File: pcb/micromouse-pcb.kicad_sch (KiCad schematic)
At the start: 40 parts, among them J2 Conn_01x06_EncoderSocket, M1 Motor_DC, Q1 BS170, Q2 TEFT4300, Q3 BS170, Q4 TEFT4300, Q5 BS170, Q6 TEFT4300, Q7 BS170, Q8 TEFT4300, SW1 SW_SPDT, U0 Teensy 4.1, U1 L7805, U2 DRV8833PWP

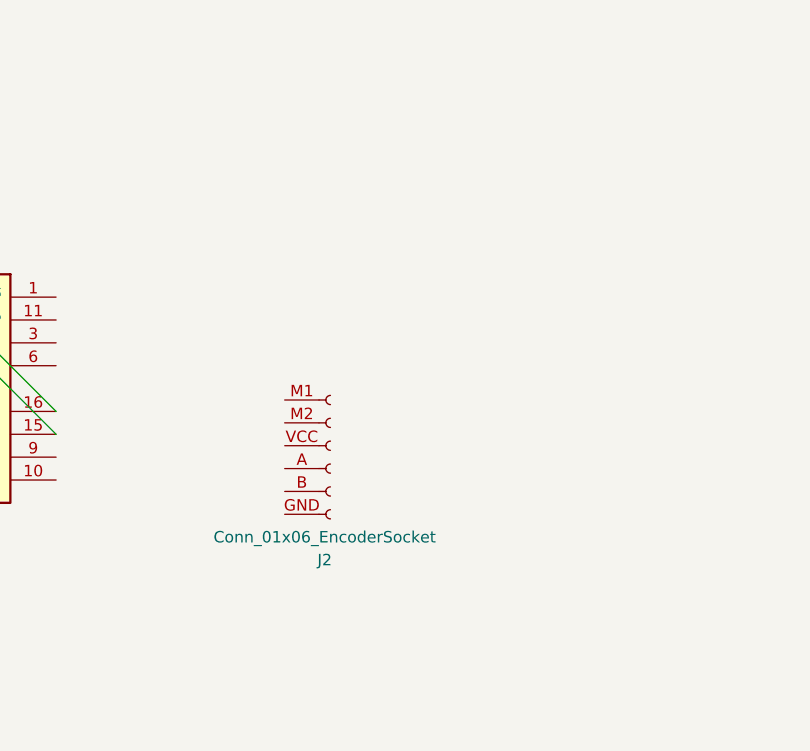
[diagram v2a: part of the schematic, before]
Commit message: changed connectors in motor module
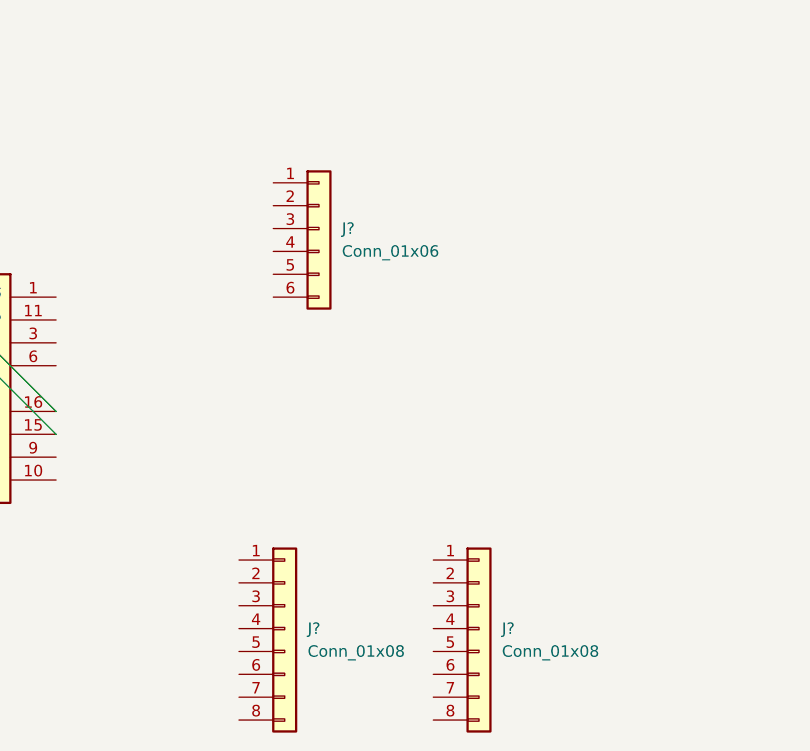
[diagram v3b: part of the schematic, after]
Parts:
- removed J2: Conn_01x06_EncoderSocket, symbol micromouse-symbols:Conn_01x06_EncoderSocket
- added J?: Conn_01x06, symbol Connector_Generic:Conn_01x06
- added J? (x2): Conn_01x08, symbol Connector_Generic:Conn_01x08
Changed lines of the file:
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@@
 	)
 	(symbol
+		(lib_id "Connector_Generic:Conn_01x06")
+		(at 146.05 223.52 0)
+		(unit 1)
+		(exclude_from_sim no)
+		(in_bom yes)
+		(on_board yes)
+		(dnp no)
+		(fields_autoplaced yes)
+		(property "Reference" "J?"
+			(at 148.59 223.5199 0)
+			(effects
+				(font
+					(size 1.27 1.27)
+				)
+				(justify left)
+			)
+		)
+		(property "Value" "Conn_01x06"
+			(at 148.59 226.0599 0)
+			(effects
+				(font
+					(size 1.27 1.27)
+				)
+				(justify left)
+			)
+		)
+		(property "Footprint" ""
+			(at 146.05 223.52 0)
+			(effects
+				(font
+					(size 1.27 1.27)
+				)
+				(hide yes)
+			)
+		)
+		(property "Datasheet" "~"
+			(at 146.05 223.52 0)
+			(effects
+				(font
+					(size 1.27 1.27)
+				)
+				(hide yes)
+			)
+		)
+		(property "Description" "Generic connector, single row, 01x06, script generated (kicad-library-utils/schlib/autogen/connector/)"
+			(at 146.05 223.52 0)
+			(effects
+				(font
+					(size 1.27 1.27)
+				)
+				(hide yes)
+			)
+		)
+		(pin "1"
+		)
+		(pin "4"
+		)
+		(pin "2"
+		)
+		(pin "6"
+		)
+		(pin "5"
+		)
+		(pin "3"
+		)
+		(instances
+			(project ""
+				(path "/6bab3514-b9e6-4652-bd2e-edc57bdbde3d"
+					(reference "J?")
+					(unit 1)
+				)
+			)
+		)
+	)
+	(symbol
 		(lib_id "Regulator_Linear:L7805")
 		(at 346.71 46.99 0)
@@
 	)
 	(symbol
-		(lib_id "micromouse-symbols:Conn_01x06_EncoderSocket")
-		(at 147.32 247.65 0)
+		(lib_id "Transistor_FET:BS170")
+		(at 361.95 120.65 90)
 		(unit 1)
 		(exclude_from_sim no)
@@
 		(on_board yes)
 		(dnp no)
-		(property "Reference" "J2"
-			(at 146.685 260.35 0)
+		(fields_autoplaced yes)
+		(property "Reference" "Q1"
+			(at 361.95 111.76 90)
 			(effects
 				(font
@@
 			)
 		)
-		(property "Value" "Conn_01x06_EncoderSocket"
-			(at 146.685 257.81 0)
+		(property "Value" "BS170"
+			(at 361.95 114.3 90)
 			(effects
 				(font
@@
 			)
 		)
-		(property "Footprint" ""
-			(at 147.32 247.65 0)
+		(property "Footprint" "Package_TO_SOT_THT:TO-92_Inline"
+			(at 363.855 115.57 0)
 			(effects
 				(font
 					(size 1.27 1.27)
+					(italic yes)
 				)
+				(justify left)
 				(hide yes)
 			)
 		)
-		(property "Datasheet" "~"
-			(at 147.32 247.65 0)
+		(property "Datasheet" "https://www.onsemi.com/pub/Collateral/BS170-D.PDF"
+			(at 365.76 115.57 0)
 			(effects
 				(font
 					(size 1.27 1.27)
 				)
+				(justify left)
 				(hide yes)
 			)
 		)
-		(property "Description" "Generic connector, single row, 01x06, script generated"
-			(at 147.32 247.65 0)
+		(property "Description" "0.5A Id, 60V Vds, N-Channel MOSFET, TO-92"
+			(at 361.95 120.65 0)
 			(effects
 				(font
@@
 			)
 		)
-		(pin "A"
-		)
-		(pin "B"
-		)
-		(pin "GND"
-		)
-		(pin "M1"
+		(pin "1"
 		)
-		(pin "M2"
+		(pin "2"
 		)
-		(pin "VCC"
+		(pin "3"
 		)
 		(instances
 			(project ""
 				(path "/6bab3514-b9e6-4652-bd2e-edc57bdbde3d"
-					(reference "J2")
+					(reference "Q1")
 					(unit 1)
 				)
@@
 	)
 	(symbol
-		(lib_id "Transistor_FET:BS170")
-		(at 361.95 120.65 90)
+		(lib_id "power:GND")
+		(at 346.71 59.69 0)
 		(unit 1)
 		(exclude_from_sim no)
@@
 		(dnp no)
 		(fields_autoplaced yes)
-		(property "Reference" "Q1"
-			(at 361.95 111.76 90)
+		(property "Reference" "#PWR01"
+			(at 346.71 66.04 0)
 			(effects
 				(font
 					(size 1.27 1.27)
 				)
+				(hide yes)
 			)
 		)
-		(property "Value" "BS170"
-			(at 361.95 114.3 90)
+		(property "Value" "GND"
+			(at 349.25 60.9599 0)
 			(effects
 				(font
 					(size 1.27 1.27)
 				)
+				(justify left)
 			)
 		)
-		(property "Footprint" "Package_TO_SOT_THT:TO-92_Inline"
-			(at 363.855 115.57 0)
+		(property "Footprint" ""
+			(at 346.71 59.69 0)
 			(effects
 				(font
 					(size 1.27 1.27)
-					(italic yes)
 				)
-				(justify left)
 				(hide yes)
 			)
 		)
-		(property "Datasheet" "https://www.onsemi.com/pub/Collateral/BS170-D.PDF"
-			(at 365.76 115.57 0)
+		(property "Datasheet" ""
+			(at 346.71 59.69 0)
 			(effects
 				(font
 					(size 1.27 1.27)
 				)
-				(justify left)
 				(hide yes)
 			)
 		)
-		(property "Description" "0.5A Id, 60V Vds, N-Channel MOSFET, TO-92"
-			(at 361.95 120.65 0)
+		(property "Description" "Power symbol creates a global label with name \"GND\" , ground"
+			(at 346.71 59.69 0)
 			(effects
 				(font
@@
 		(pin "1"
 		)
-		(pin "2"
-		)
-		(pin "3"
-		)
 		(instances
 			(project ""
 				(path "/6bab3514-b9e6-4652-bd2e-edc57bdbde3d"
-					(reference "Q1")
+					(reference "#PWR01")
 					(unit 1)
 				)
@@
 	)
 	(symbol
-		(lib_id "power:GND")
-		(at 346.71 59.69 0)
+		(lib_id "Connector_Generic:Conn_01x08")
+		(at 163.83 267.97 0)
 		(unit 1)
 		(exclude_from_sim no)
@@
 		(dnp no)
 		(fields_autoplaced yes)
-		(property "Reference" "#PWR01"
-			(at 346.71 66.04 0)
+		(property "Reference" "J?"
+			(at 166.37 267.9699 0)
 			(effects
 				(font
 					(size 1.27 1.27)
 				)
-				(hide yes)
+				(justify left)
 			)
 		)
-		(property "Value" "GND"
-			(at 349.25 60.9599 0)
+		(property "Value" "Conn_01x08"
+			(at 166.37 270.5099 0)
 			(effects
 				(font
@@
 		)
 		(property "Footprint" ""
-			(at 346.71 59.69 0)
+			(at 163.83 267.97 0)
 			(effects
 				(font
@@
 			)
 		)
-		(property "Datasheet" ""
-			(at 346.71 59.69 0)
+		(property "Datasheet" "~"
+			(at 163.83 267.97 0)
 			(effects
 				(font
@@
 			)
 		)
-		(property "Description" "Power symbol creates a global label with name \"GND\" , ground"
-			(at 346.71 59.69 0)
+		(property "Description" "Generic connector, single row, 01x08, script generated (kicad-library-utils/schlib/autogen/connector/)"
+			(at 163.83 267.97 0)
 			(effects
 				(font
@@
 			)
 		)
+		(pin "2"
+		)
+		(pin "3"
+		)
+		(pin "4"
+		)
+		(pin "5"
+		)
+		(pin "6"
+		)
+		(pin "7"
+		)
+		(pin "8"
+		)
 		(pin "1"
 		)
@@
 			(project ""
 				(path "/6bab3514-b9e6-4652-bd2e-edc57bdbde3d"
-					(reference "#PWR01")
+					(reference "J?")
 					(unit 1)
 				)
@@
 					(unit 1)
 				)
+			)
+		)
+	)
+	(symbol
+		(lib_id "Connector_Generic:Conn_01x08")
+		(at 142.24 267.97 0)
+		(unit 1)
+		(exclude_from_sim no)
+		(in_bom yes)
+		(on_board yes)
+		(dnp no)
+		(fields_autoplaced yes)
+		(property "Reference" "J?"
+			(at 144.78 267.9699 0)
+			(effects
+				(font
+					(size 1.27 1.27)
+				)
+				(justify left)
+			)
+		)
+		(property "Value" "Conn_01x08"
+			(at 144.78 270.5099 0)
+			(effects
+				(font
+					(size 1.27 1.27)
+				)
+				(justify left)
+			)
+		)
+		(property "Footprint" ""
+			(at 142.24 267.97 0)
+			(effects
+				(font
+					(size 1.27 1.27)
+				)
+				(hide yes)
+			)
+		)
+		(property "Datasheet" "~"
+			(at 142.24 267.97 0)
+			(effects
+				(font
+					(size 1.27 1.27)
+				)
+				(hide yes)
+			)
+		)
+		(property "Description" "Generic connector, single row, 01x08, script generated (kicad-library-utils/schlib/autogen/connector/)"
+			(at 142.24 267.97 0)
+			(effects
+				(font
+					(size 1.27 1.27)
+				)
+				(hide yes)
+			)
+		)
+		(pin "2"
+		)
+		(pin "3"
+		)
+		(pin "4"
+		)
+		(pin "5"
+		)
+		(pin "6"
+		)
+		(pin "7"
+		)
+		(pin "8"
+		)
+		(pin "1"
+		)
+		(instances
+			(project "micromouse-pcb"
+				(path "/6bab3514-b9e6-4652-bd2e-edc57bdbde3d"
+					(reference "J?")
+					(unit 1)
+				)

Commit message: schematic not updating?
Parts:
- gave numbers to parts that had none: 3
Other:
- moved on the sheet: J2, J3
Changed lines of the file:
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@@
 		(dnp no)
 		(fields_autoplaced yes)
-		(property "Reference" "J?"
+		(property "Reference" "J1"
 			(at 148.59 223.5199 0)
 			(effects
@@
 			(project ""
 				(path "/6bab3514-b9e6-4652-bd2e-edc57bdbde3d"
-					(reference "J?")
+					(reference "J1")
 					(unit 1)
 				)
@@
 	(symbol
 		(lib_id "Connector_Generic:Conn_01x08")
-		(at 163.83 267.97 0)
+		(at 168.91 254 0)
 		(unit 1)
 		(exclude_from_sim no)
@@
 		(dnp no)
 		(fields_autoplaced yes)
-		(property "Reference" "J?"
-			(at 166.37 267.9699 0)
+		(property "Reference" "J3"
+			(at 171.45 253.9999 0)
 			(effects
 				(font
@@
 		)
 		(property "Value" "Conn_01x08"
-			(at 166.37 270.5099 0)
+			(at 171.45 256.5399 0)
 			(effects
 				(font
@@
 		)
 		(property "Footprint" ""
-			(at 163.83 267.97 0)
+			(at 168.91 254 0)
 			(effects
 				(font
@@
 		)
 		(property "Datasheet" "~"
-			(at 163.83 267.97 0)
+			(at 168.91 254 0)
 			(effects
 				(font
@@
 		)
 		(property "Description" "Generic connector, single row, 01x08, script generated (kicad-library-utils/schlib/autogen/connector/)"
-			(at 163.83 267.97 0)
+			(at 168.91 254 0)
 			(effects
 				(font
@@
 			(project ""
 				(path "/6bab3514-b9e6-4652-bd2e-edc57bdbde3d"
-					(reference "J?")
+					(reference "J3")
 					(unit 1)
 				)
@@
 	(symbol
 		(lib_id "Connector_Generic:Conn_01x08")
-		(at 142.24 267.97 0)
+		(at 142.24 254 0)
 		(unit 1)
 		(exclude_from_sim no)
@@
 		(dnp no)
 		(fields_autoplaced yes)
-		(property "Reference" "J?"
-			(at 144.78 267.9699 0)
+		(property "Reference" "J2"
+			(at 144.78 253.9999 0)
 			(effects
 				(font
@@
 		)
 		(property "Value" "Conn_01x08"
-			(at 144.78 270.5099 0)
+			(at 144.78 256.5399 0)
 			(effects
 				(font
@@
 		)
 		(property "Footprint" ""
-			(at 142.24 267.97 0)
+			(at 142.24 254 0)
 			(effects
 				(font
@@
 		)
 		(property "Datasheet" "~"
-			(at 142.24 267.97 0)
+			(at 142.24 254 0)
 			(effects
 				(font
@@
 		)
 		(property "Description" "Generic connector, single row, 01x08, script generated (kicad-library-utils/schlib/autogen/connector/)"
-			(at 142.24 267.97 0)
+			(at 142.24 254 0)
 			(effects
 				(font
@@
 			(project "micromouse-pcb"
 				(path "/6bab3514-b9e6-4652-bd2e-edc57bdbde3d"
-					(reference "J?")
+					(reference "J2")
 					(unit 1)
 				)

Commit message: worked a bit on motor module
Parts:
- removed M1: Motor_DC, symbol Motor:Motor_DC
- removed U2: DRV8833PWP, Package_SO:HTSSOP-16-1EP_4.4x5mm_P0.65mm_EP3.4x5mm_Mask2.46x2.31mm_ThermalVias, symbol Driver_Motor:DRV8833PWP
- removed U6: ~, symbol micromouse-symbols:Polulu_Encoder
- added J?: Conn_01x06, symbol Connector_Generic:Conn_01x06
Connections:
- net 3.3V: now also J1.4 (Pin_4)
- net GND: now also J1.1 (Pin_1), J2.8 (Pin_8), J3.3 (Pin_3), J3.8 (Pin_8)
- net Logic M1_A: now reaches J1.2 (Pin_2)
- net Logic M1_A: now also J2.3 (Pin_3)
- net Logic M1_B: now reaches J1.3 (Pin_3)
- net Logic M1_B: now also J2.2 (Pin_2)
- net M1_A: now reaches J1.5 (Pin_5)
- net M1_A: now also J3.4 (Pin_4)
- net M1_B: now reaches J1.6 (Pin_6)
- net M1_B: now also J3.5 (Pin_5)
- net M2_B: now reaches J3.6 (Pin_6)
- net M2_A: now reaches J3.7 (Pin_7)
- no-connect marks 1 -> 4
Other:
- moved on the sheet: J1, J2, J3

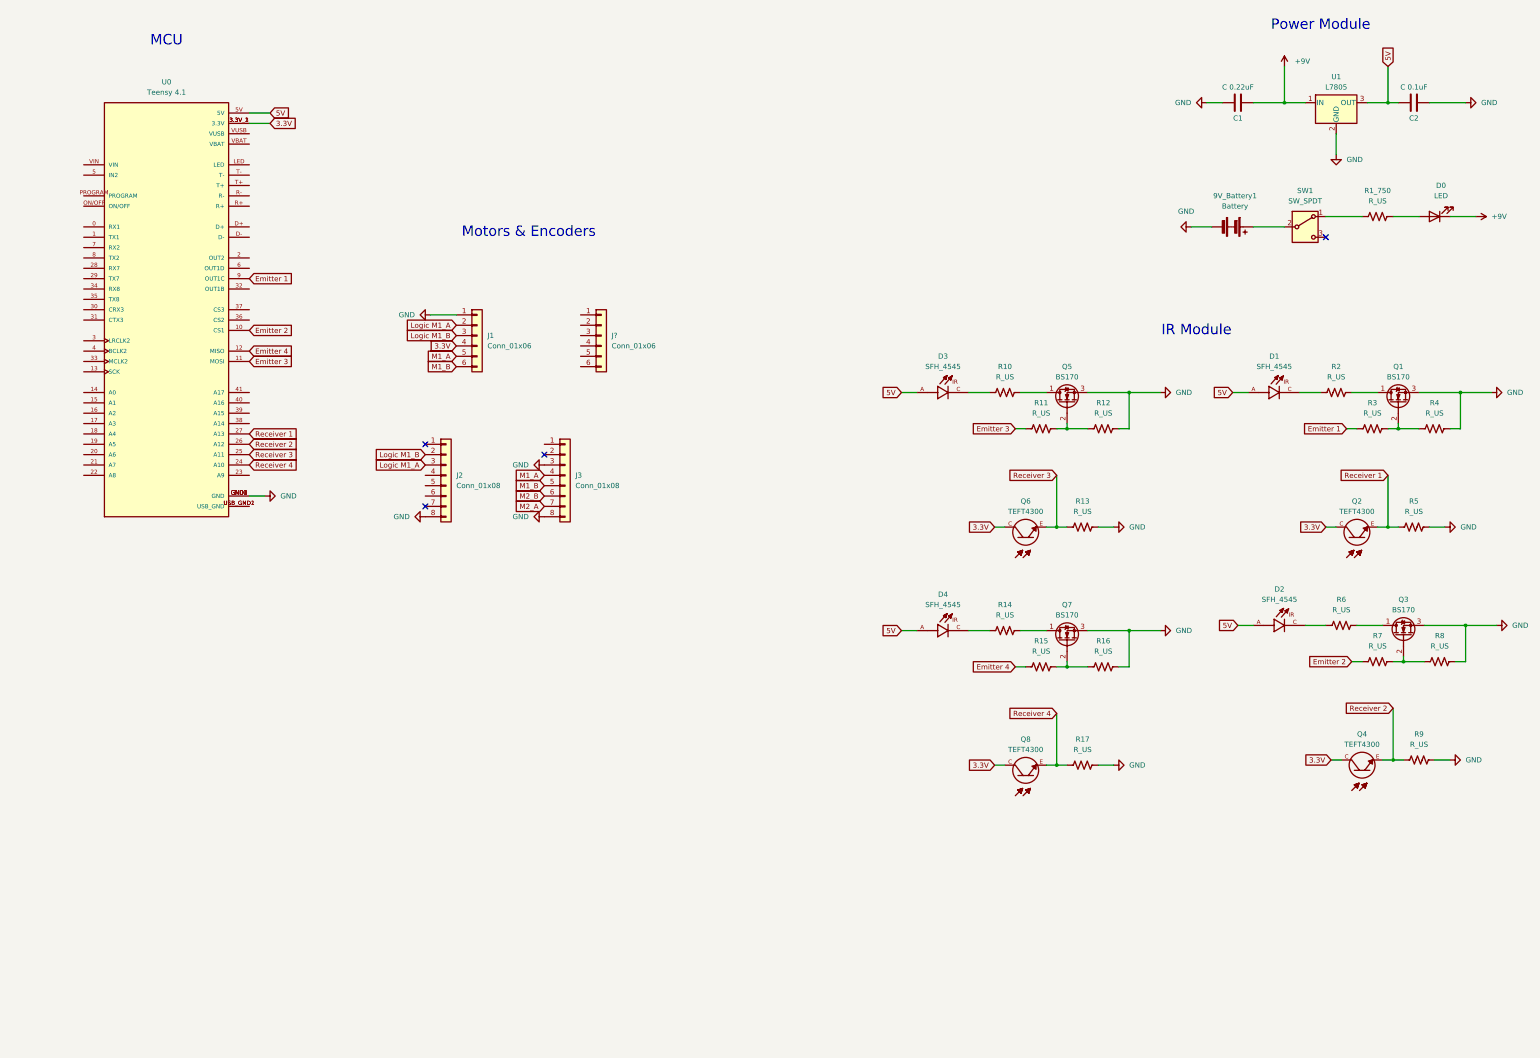
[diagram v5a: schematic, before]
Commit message: finished motor module
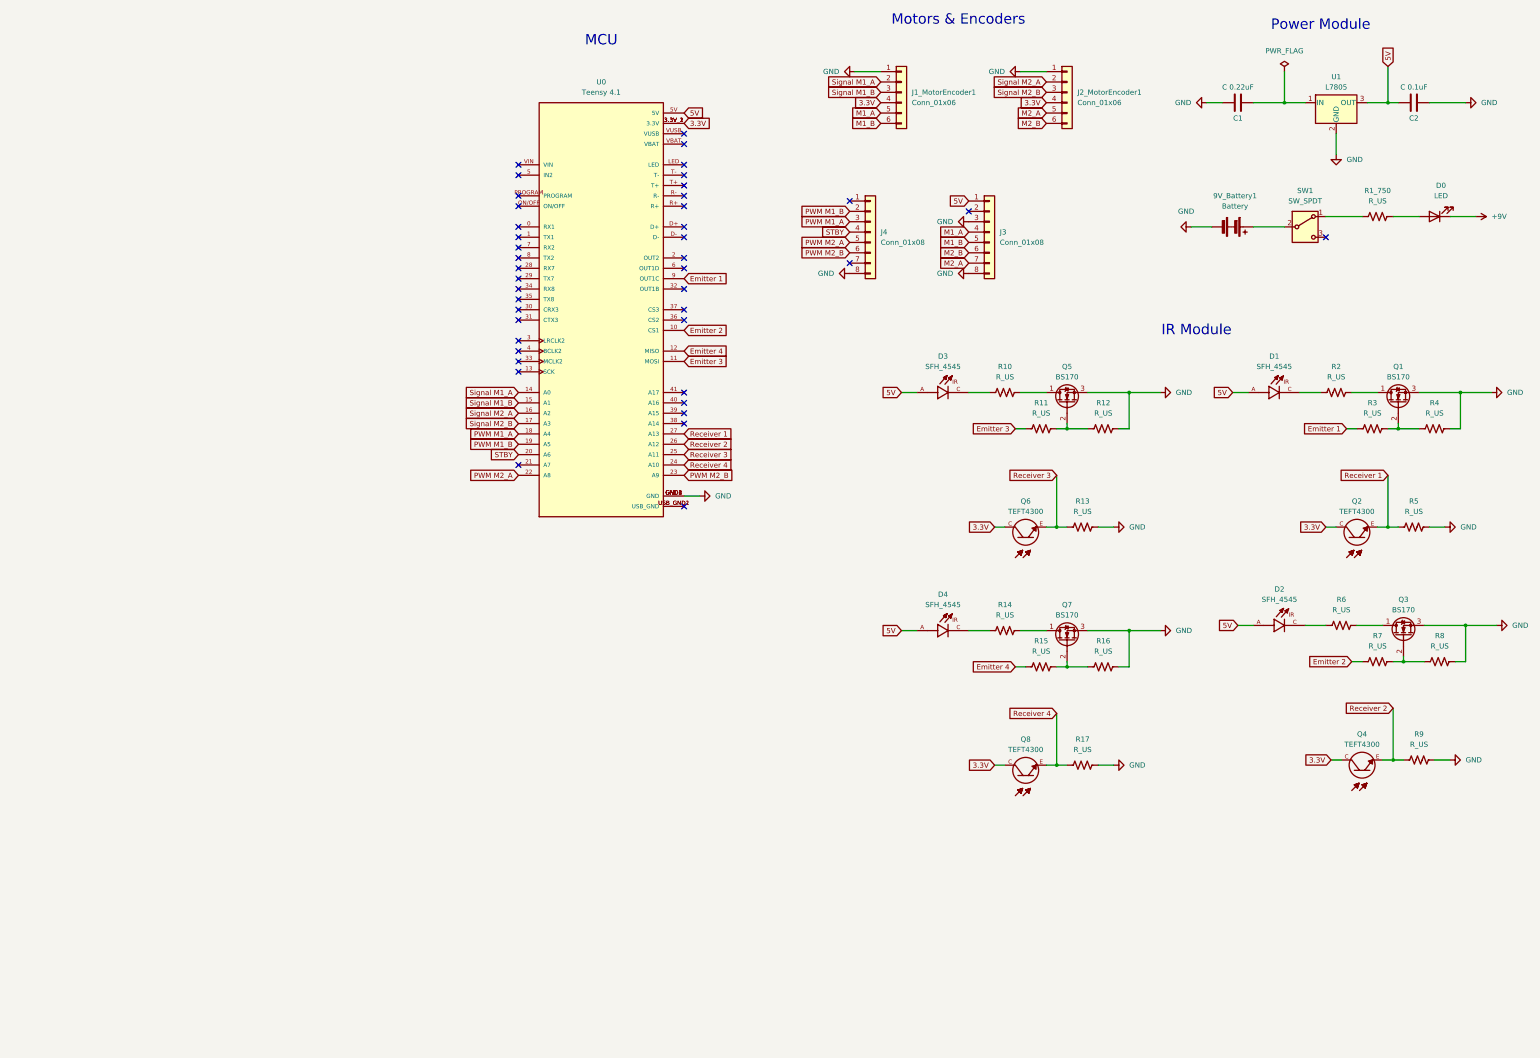
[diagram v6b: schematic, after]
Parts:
- removed J?: Conn_01x06, symbol Connector_Generic:Conn_01x06
- added J2_MotorEncoder1: Conn_01x06, symbol Connector_Generic:Conn_01x06
- C1, C2: footprint (none) -> Capacitor_SMD:C_0805_2012Metric_Pad1.18x1.45mm_HandSolder
- R10, R11, R12, R13, R14, R15, R16, R17, R1_750, R2, R3, R4, R5, R6, R7, R8, R9: footprint (none) -> Resistor_SMD:R_0805_2012Metric_Pad1.20x1.40mm_HandSolder
- renumbered J1 to J1_MotorEncoder1, J2 to J4
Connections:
- net +9V: no longer C1.1, U1.1 (IN)
- net 3.3V: now also J2_MotorEncoder1.4 (Pin_4)
- net 5V: now also J3.1 (Pin_1)
- net GND: now also J2_MotorEncoder1.1 (Pin_1)
- net M2_A: now also J2_MotorEncoder1.5 (Pin_5)
- net M2_B: now also J2_MotorEncoder1.6 (Pin_6)
- net Signal M1_A: now reaches U0.14 (A0)
- net Signal M1_A: now also J1_MotorEncoder1.2 (Pin_2)
- net Signal M1_B: now reaches U0.15 (A1)
- net Signal M1_B: now also J1_MotorEncoder1.3 (Pin_3)
- net Signal M2_A: now reaches U0.16 (A2)
- net Signal M2_A: now also J2_MotorEncoder1.2 (Pin_2)
- net Signal M2_B: now reaches U0.17 (A3)
- net Signal M2_B: now also J2_MotorEncoder1.3 (Pin_3)
- net PWM M1_A: now reaches U0.18 (A4)
- net PWM M1_A: now also J4.3 (Pin_3)
- net PWM M1_B: now reaches U0.19 (A5)
- net PWM M1_B: now also J4.2 (Pin_2)
- net STBY: now reaches U0.20 (A6)
- net STBY: now also J4.4 (Pin_4)
- net PWM M2_A: now reaches U0.22 (A8)
- net PWM M2_A: now also J4.5 (Pin_5)
- net PWM M2_B: now reaches U0.23 (A9)
- net PWM M2_B: now also J4.6 (Pin_6)
- removed net Logic M1_A: J1_MotorEncoder1.2 (Pin_2), J4.3 (Pin_3)
- removed net Logic M1_B: J1_MotorEncoder1.3 (Pin_3), J4.2 (Pin_2)
- new net: C1.1, U1.1 (IN)
- no-connect marks 4 -> 42
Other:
- moved on the sheet: J1_MotorEncoder1, J3, J4, U0
